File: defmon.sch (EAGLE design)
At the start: 18 parts, among them IC2 MEGA8-P, Q1 20MHz, X1 MAB5SH, X2 1503_09

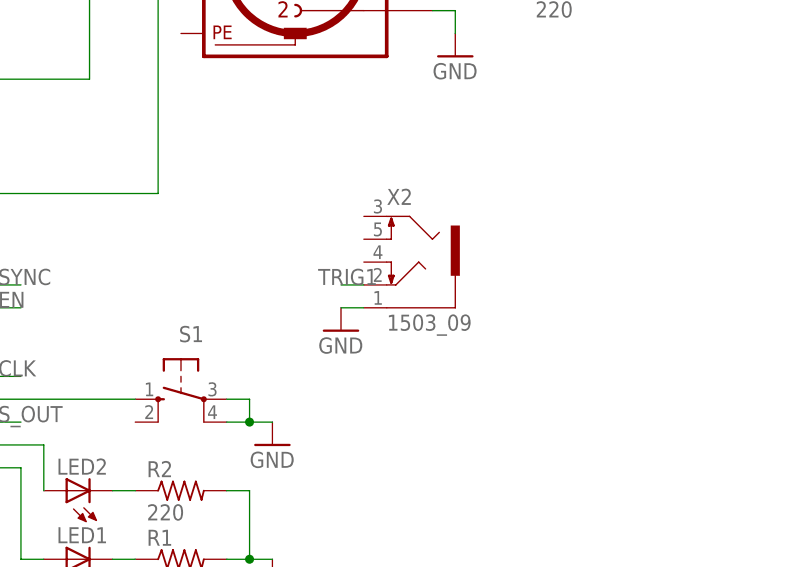
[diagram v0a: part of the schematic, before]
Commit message: added a new jack socket
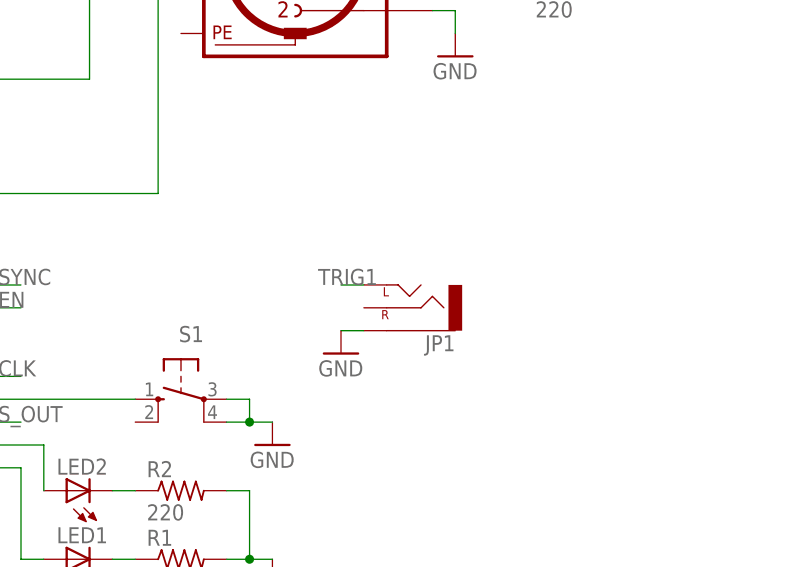
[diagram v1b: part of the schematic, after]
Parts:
- removed X2: 1503_09, con-lumberg:1503_09
- added JP1: (no value), SparkFun-Connectors:AUDIO-JACKPTH
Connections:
- net GND: now also JP1.SLEEVE; no longer X2.1
- net TRIG1: now also JP1.LEFT; no longer X2.2
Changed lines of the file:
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@@
 <layer number="54" name="bGND_GNDA" color="1" fill="9" visible="no" active="no"/>
 <layer number="56" name="wert" color="7" fill="1" visible="no" active="no"/>
+<layer number="57" name="tCAD" color="7" fill="1" visible="no" active="no"/>
+<layer number="90" name="Modules" color="5" fill="1" visible="yes" active="yes"/>
 <layer number="91" name="Nets" color="2" fill="1" visible="yes" active="yes"/>
 <layer number="92" name="Busses" color="1" fill="1" visible="yes" active="yes"/>
@@
 <layer number="97" name="Info" color="7" fill="1" visible="yes" active="yes"/>
 <layer number="98" name="Guide" color="6" fill="1" visible="yes" active="yes"/>
+<layer number="99" name="SpiceOrder" color="7" fill="1" visible="yes" active="yes"/>
 <layer number="100" name="Muster" color="7" fill="1" visible="no" active="no"/>
 <layer number="101" name="Patch_Top" color="12" fill="4" visible="yes" active="yes"/>
@@
 <layer number="106" name="bPlate" color="7" fill="1" visible="yes" active="yes"/>
 <layer number="107" name="Crop" color="7" fill="1" visible="yes" active="yes"/>
+<layer number="108" name="tplace-old" color="10" fill="1" visible="yes" active="yes"/>
+<layer number="109" name="ref-old" color="11" fill="1" visible="yes" active="yes"/>
+<layer number="110" name="fp0" color="7" fill="1" visible="yes" active="yes"/>
+<layer number="111" name="LPC17xx" color="7" fill="1" visible="yes" active="yes"/>
+<layer number="112" name="tSilk" color="7" fill="1" visible="yes" active="yes"/>
+<layer number="113" name="IDFDebug" color="4" fill="1" visible="yes" active="yes"/>
 <layer number="116" name="Patch_BOT" color="9" fill="4" visible="yes" active="yes"/>
 <layer number="121" name="_tsilk" color="7" fill="1" visible="yes" active="yes"/>
 <layer number="122" name="_bsilk" color="7" fill="1" visible="yes" active="yes"/>
+<layer number="123" name="tTestmark" color="7" fill="1" visible="yes" active="yes"/>
+<layer number="124" name="bTestmark" color="7" fill="1" visible="yes" active="yes"/>
 <layer number="125" name="_tNames" color="7" fill="1" visible="yes" active="yes"/>
+<layer number="126" name="_bNames" color="7" fill="1" visible="yes" active="yes"/>
+<layer number="127" name="_tValues" color="7" fill="1" visible="yes" active="yes"/>
+<layer number="128" name="_bValues" color="7" fill="1" visible="yes" active="yes"/>
+<layer number="131" name="tAdjust" color="7" fill="1" visible="yes" active="yes"/>
+<layer number="132" name="bAdjust" color="7" fill="1" visible="yes" active="yes"/>
 <layer number="144" name="Drill_legend" color="7" fill="1" visible="yes" active="yes"/>
+<layer number="150" name="Notes" color="7" fill="1" visible="yes" active="yes"/>
 <layer number="151" name="HeatSink" color="7" fill="1" visible="yes" active="yes"/>
+<layer number="152" name="_bDocu" color="7" fill="1" visible="yes" active="yes"/>
+<layer number="153" name="FabDoc1" color="7" fill="1" visible="yes" active="yes"/>
+<layer number="154" name="FabDoc2" color="7" fill="1" visible="yes" active="yes"/>
+<layer number="155" name="FabDoc3" color="7" fill="1" visible="yes" active="yes"/>
 <layer number="199" name="Contour" color="7" fill="1" visible="yes" active="yes"/>
 <layer number="200" name="200bmp" color="1" fill="10" visible="yes" active="yes"/>
@@
 <layer number="223" name="223bmp" color="24" fill="1" visible="no" active="no"/>
 <layer number="224" name="224bmp" color="25" fill="1" visible="no" active="no"/>
+<layer number="248" name="Housing" color="7" fill="1" visible="yes" active="yes"/>
+<layer number="249" name="Edge" color="7" fill="1" visible="yes" active="yes"/>
 <layer number="250" name="Descript" color="3" fill="1" visible="no" active="no"/>
 <layer number="251" name="SMDround" color="12" fill="11" visible="no" active="no"/>
@@
 <part name="GND6" library="supply1" deviceset="GND" device=""/>
 <part name="GND7" library="supply1" deviceset="GND" device=""/>
-<part name="X2" library="con-lumberg" deviceset="1503_09" device=""/>
 <part name="GND8" library="supply1" deviceset="GND" device=""/>
 <part name="GND1" library="supply1" deviceset="GND" device=""/>
@@
 <part name="GND10" library="supply1" deviceset="GND" device=""/>
 <part name="R4" library="rcl" deviceset="R-US_" device="0204/7" value="10k"/>
+<part name="JP1" library="SparkFun-Connectors" deviceset="AUDIO-JACK" device="PTH"/>
 </parts>
 <sheets>
@@
 <instance part="P+3" gate="VCC" x="259.08" y="238.76"/>
 <instance part="GND6" gate="1" x="226.06" y="243.84"/>
-<instance part="GND7" gate="1" x="172.72" y="190.5"/>
-<instance part="X2" gate="G$1" x="180.34" y="198.12"/>
+<instance part="GND7" gate="1" x="172.72" y="187.96"/>
 <instance part="GND8" gate="1" x="302.26" y="236.22"/>
 <instance part="GND1" gate="1" x="299.72" y="208.28"/>
@@
 <instance part="GND10" gate="1" x="66.04" y="200.66"/>
 <instance part="R4" gate="G$1" x="78.74" y="231.14"/>
+<instance part="JP1" gate="G$1" x="180.34" y="193.04" rot="R180"/>
 </instances>
 <busses>
@@
 <segment>
 <pinref part="GND7" gate="1" pin="GND"/>
-<pinref part="X2" gate="G$1" pin="1"/>
-<wire x1="172.72" y1="193.04" x2="175.26" y2="193.04" width="0.1524" layer="91"/>
+<wire x1="172.72" y1="190.5" x2="175.26" y2="190.5" width="0.1524" layer="91"/>
+<pinref part="JP1" gate="G$1" pin="SLEEVE"/>
 </segment>
 <segment>
@@
 </segment>
 <segment>
-<pinref part="X2" gate="G$1" pin="2"/>
 <wire x1="175.26" y1="195.58" x2="172.72" y2="195.58" width="0.1524" layer="91"/>
 <label x="170.18" y="195.58" size="1.778" layer="95"/>
-</segment>
-</net>
+<pinref part="JP1" gate="G$1" pin="LEFT"/>
+</segment>
+</net>
